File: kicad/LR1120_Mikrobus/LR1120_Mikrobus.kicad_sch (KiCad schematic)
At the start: 90 parts, among them Q1 NX2016SA-32M-EXS00A-CS06465, Q2 NT2016SA-32M-END4263A, Q3 NX3215SA, U1 LR1120, U2 SKY13588-460LF, U5 LIS2DE12, U7 M24128-BFMH6TG, U8 BGA524N6E6327XTSA1

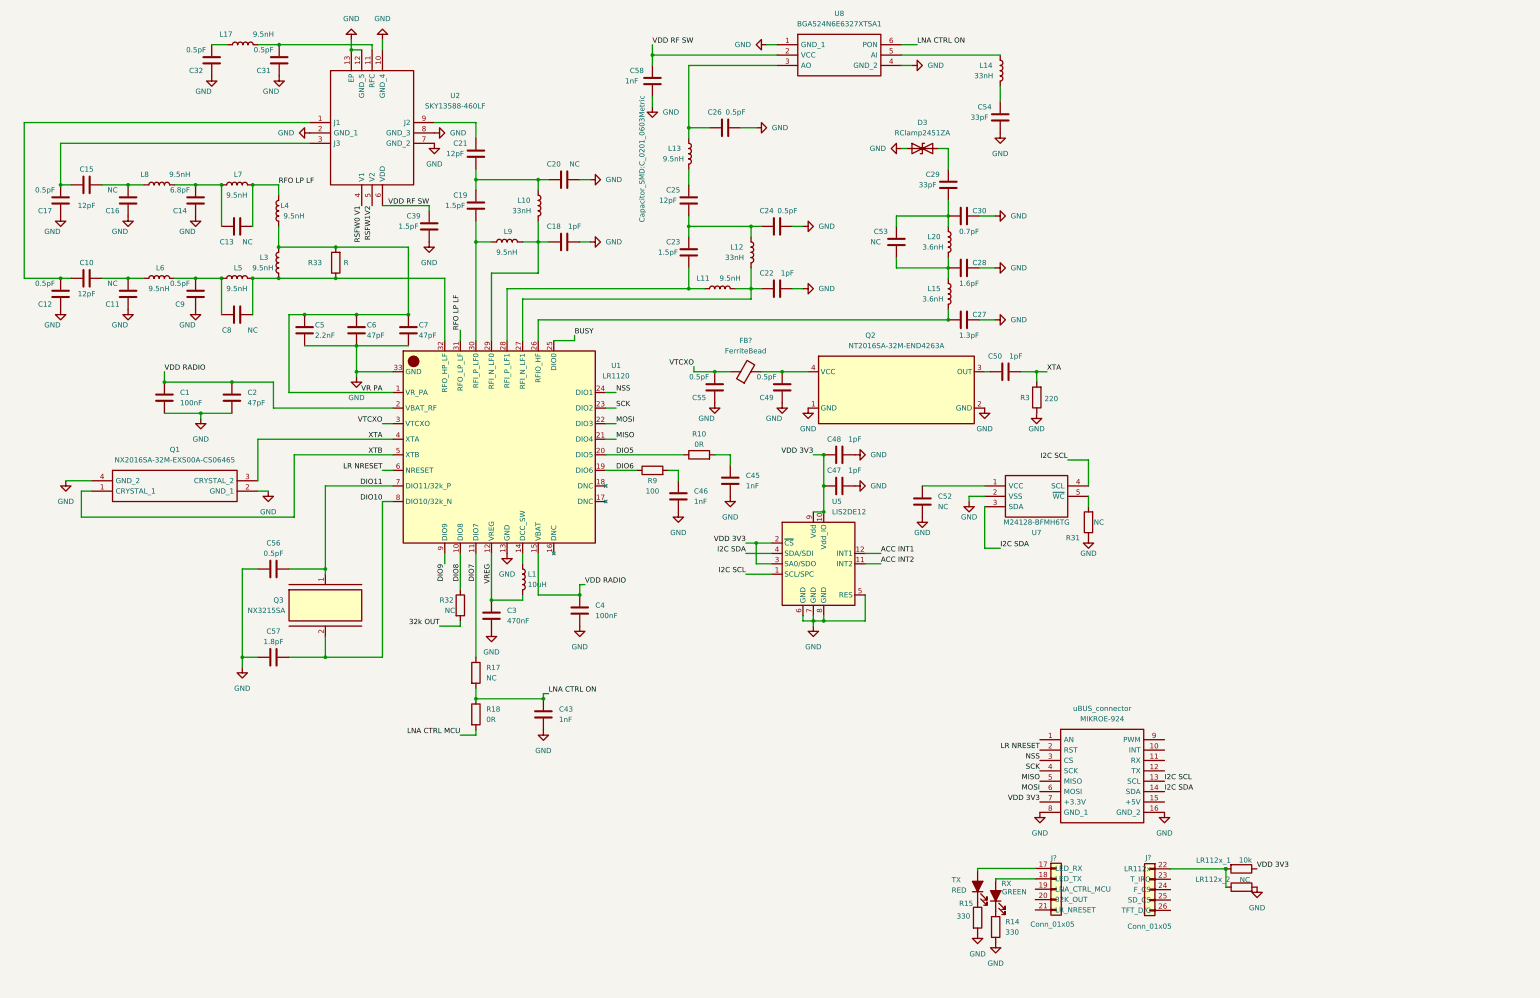
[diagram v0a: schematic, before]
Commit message: created board edges, added ant
Created board edges, placed antennas
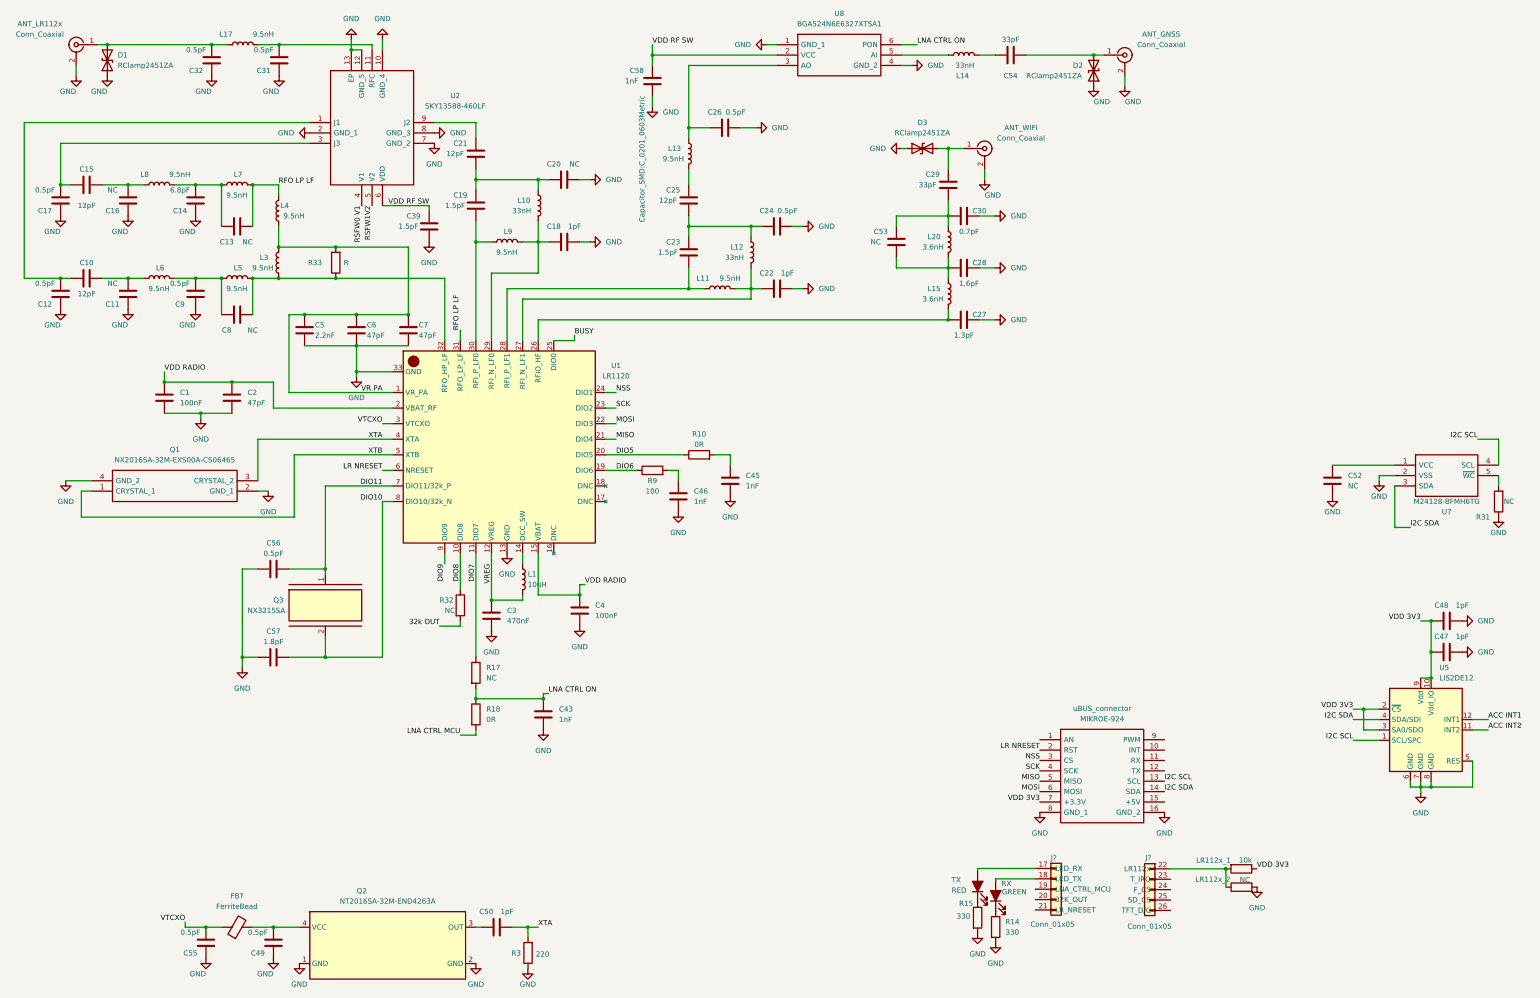
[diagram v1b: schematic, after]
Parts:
- added ANT_GNSS, ANT_LR112x, ANT_WIFI: Conn_Coaxial, Connector_Coaxial:U.FL_Hirose_U.FL-R-SMT-1_Vertical, symbol Connector:Conn_Coaxial
- added D1, D2: RClamp2451ZA, Diode_SMD:D_0201_0603Metric, symbol Device:D_TVS
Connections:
- net GND: now also ANT_GNSS.2 (Ext), ANT_LR112x.2 (Ext), ANT_WIFI.2 (Ext), D1.1 (A1), D2.1 (A1); no longer C54.1
- net at C32.1, L17.1: now also ANT_LR112x.1 (In), D1.2 (A2)
- net at C29.2, D3.2 (A2): now also ANT_WIFI.1 (In)
- new net: ANT_GNSS.1 (In), C54.1, D2.2 (A2)
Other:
- moved on the sheet: C47, C48, C49, C50, C52, C54, C55, FB?, L14, Q2, R3, R31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

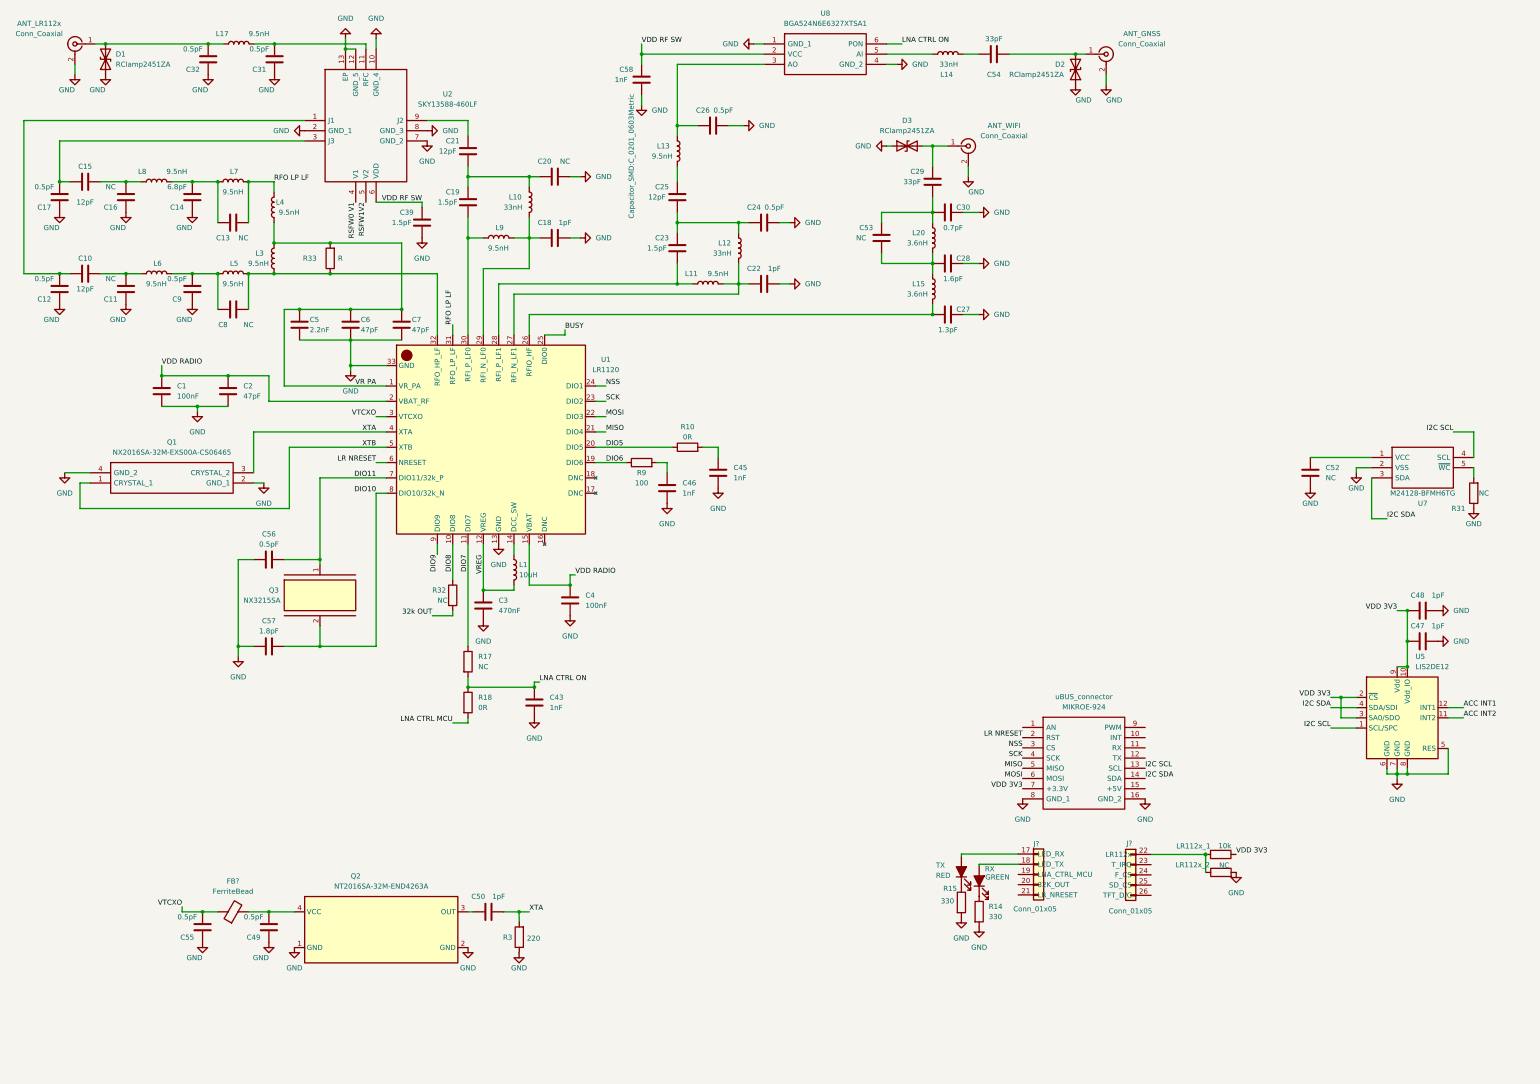
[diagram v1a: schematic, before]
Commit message: all components placed
all components have been placed. some footprints remain to be properly setup
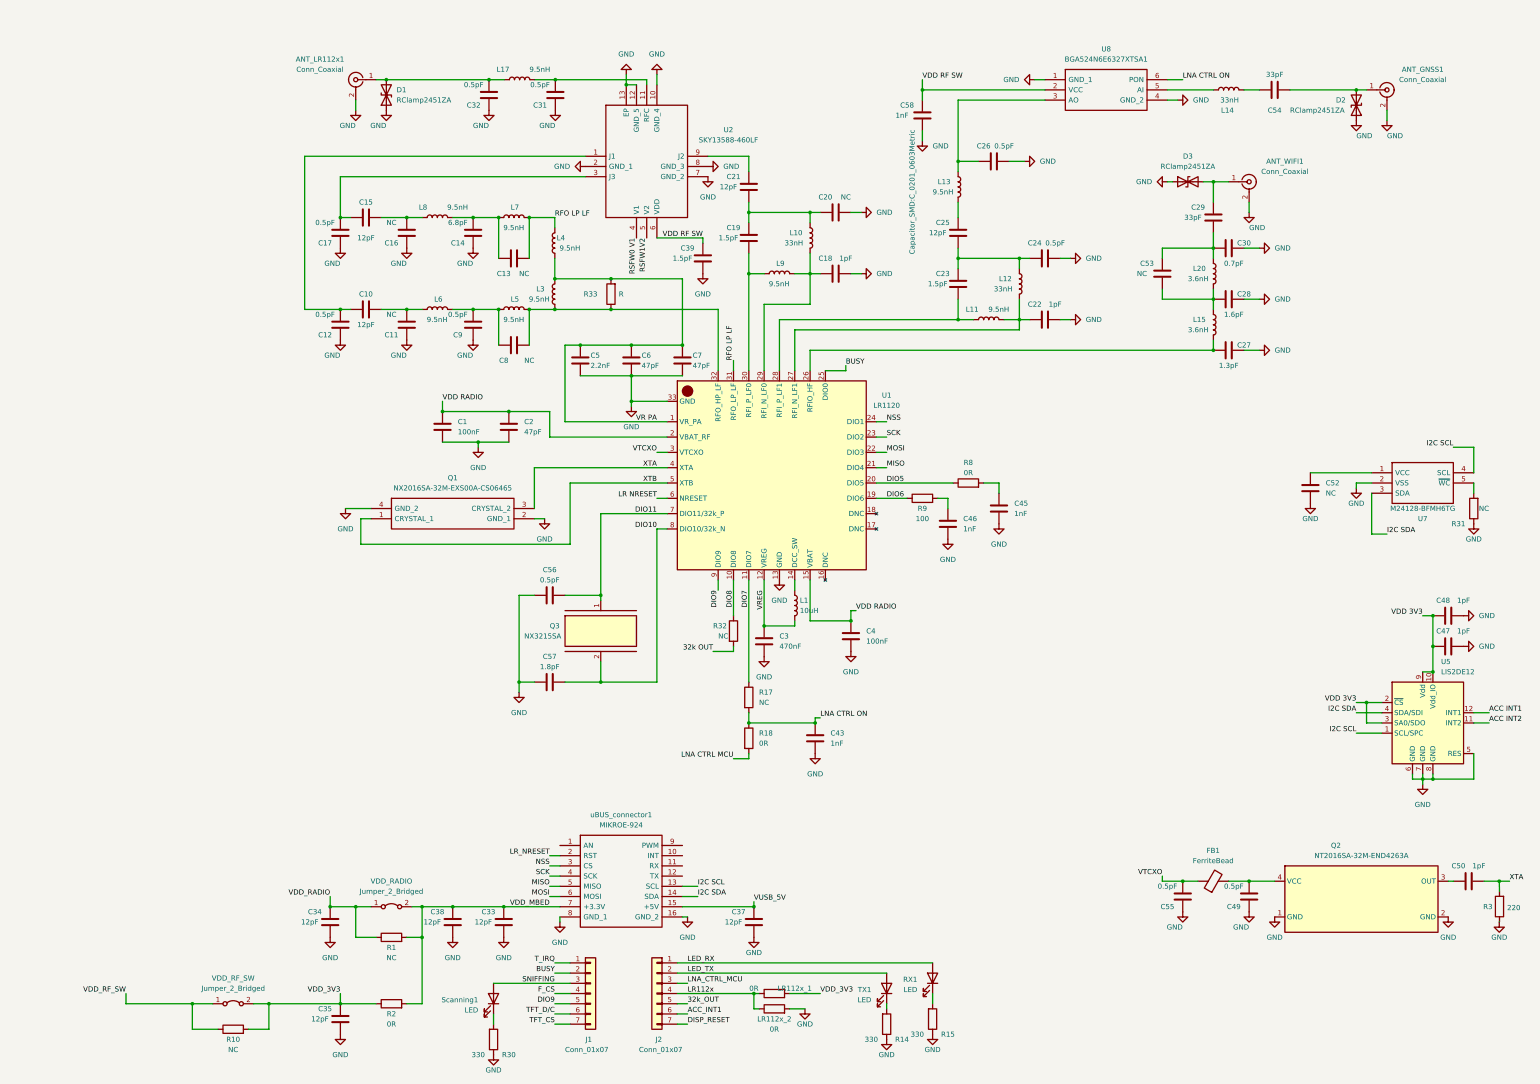
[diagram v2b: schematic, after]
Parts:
- removed J? (x2): Conn_01x05, symbol Connector_Generic:Conn_01x05
- removed RX: GREEN, symbol Device:LED_ALT
- removed TX: RED, symbol Device:LED_ALT
- added C33, C34, C35, C37, C38: 12pF, Capacitor_SMD:C_01005_0402Metric, symbol Device:C
- added J1, J2: Conn_01x07, symbol Connector_Generic:Conn_01x07
- added R1, R10: NC, Resistor_SMD:R_0201_0603Metric, symbol Device:R
- added R2: 0R, Resistor_SMD:R_0201_0603Metric, symbol Device:R
- added R30: 330, Resistor_SMD:R_0201_0603Metric, symbol Device:R
- added RX1, Scanning1, TX1: LED, symbol Device:LED
- added VDD_RADIO, VDD_RF_SW: Jumper_2_Bridged, symbol Jumper:Jumper_2_Bridged
- LR112x_1: value 10k -> 0R; footprint (none) -> Resistor_SMD:R_0603_1608Metric
- LR112x_2: value NC -> 0R; footprint (none) -> Resistor_SMD:R_0603_1608Metric
- R14, R15: footprint (none) -> Resistor_SMD:R_0201_0603Metric
- gave numbers to parts that had none: 1
- renumbered ANT_GNSS to ANT_GNSS1, ANT_LR112x to ANT_LR112x1, ANT_WIFI to ANT_WIFI1, R10 to R8, uBUS_connector to uBUS_connector1
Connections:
- net BUSY: now also J1.2 (Pin_2)
- net DIO9: now also J1.5 (Pin_5)
- net GND: now also R14.1, R15.1, C33.1, C34.1, C35.1, C37.1, C38.1, R30.1; no longer R14.2, R15.2
- net LR NRESET: no longer uBUS_connector1.2 (RST)
- net VDD 3V3: no longer LR112x_1.1, uBUS_connector1.7 (+3.3V)
- net VUSB_5V: now reaches uBUS_connector1.15 (+5V)
- net VUSB_5V: now also C37.2
- net LR112x: now reaches LR112x_2.1
- net LR112x: now also LR112x_1.1, J2.4 (Pin_4); no longer LR112x_1.2
- new net: R14.2, TX1.1 (K)
- new net: R30.2, Scanning1.1 (K)
- new net: R15.2, RX1.1 (K)
- new net 32k_OUT: J2.5 (Pin_5)
- new net ACC_INT1: J2.6 (Pin_6)
- new net DISP_RESET: J2.7 (Pin_7)
- new net F_CS: J1.4 (Pin_4)
- new net LED_RX: J2.1 (Pin_1), RX1.2 (A)
- new net LED_TX: J2.2 (Pin_2), TX1.2 (A)
- new net LNA_CTRL_MCU: J2.3 (Pin_3)
- new net LR_NRESET: uBUS_connector1.2 (RST)
- new net SNIFFING: J1.3 (Pin_3), Scanning1.2 (A)
- new net TFT_CS: J1.7 (Pin_7)
- new net TFT_D/C: J1.6 (Pin_6)
- new net T_IRQ: J1.1 (Pin_1)
- new net VDD_3V3: C35.2, LR112x_1.2, R10.2, R2.1, VDD_RF_SW.2 (B)
- new net VDD_MBED: C33.2, C38.2, R1.2, R2.2, VDD_RADIO.2 (B), uBUS_connector1.7 (+3.3V)
- new net VDD_RADIO: C34.2, R1.1, VDD_RADIO.1 (A)
- new net VDD_RF_SW: R10.1, VDD_RF_SW.1 (A)
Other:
- moved on the sheet: ANT_GNSS1, ANT_LR112x1, ANT_WIFI1, C1, C10, C11, C12, C13, C14, C15, C16, C17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

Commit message: all footprints assigned
All footprints were properly assingned according to the original BOM.
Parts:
- added R5, R6: NC, Resistor_SMD:R_0201_0603Metric, symbol Device:R
- C10, C11, C12, C13, C14, C15, C16, C17, C18, C19, C20, C21, C22, C23, C24, C25, C26, C27, C28, C29, C30, C31, C32, C34, C35, C37, C48, C8, C9: footprint Capacitor_SMD:C_01005_0402Metric -> Capacitor_SMD:C_0402_1005Metric
- C33, C39, C47, C49, C50, C53, C54, C55: footprint Capacitor_SMD:C_01005_0402Metric -> Capacitor_SMD:C_0201_0603Metric
- C38: footprint Capacitor_SMD:C_01005_0402Metric -> Capacitor_SMD:C_0603_1608Metric
- FB1: footprint (none) -> Inductor_SMD:L_0201_0603Metric
- J1, J2: footprint (none) -> Connector_PinHeader_2.54mm:PinHeader_1x07_P2.54mm_Vertical
- L10, L11, L12, L13, L15, L17, L20, L3, L4, L5, L6, L7, L8, L9: footprint Inductor_SMD:L_01005_0402Metric -> Inductor_SMD:L_0402_1005Metric
- L14: footprint Inductor_SMD:L_01005_0402Metric -> Inductor_SMD:L_0201_0603Metric
- LR112x_1, LR112x_2: footprint Resistor_SMD:R_0603_1608Metric -> Resistor_SMD:R_0402_1005Metric
- R1, R10, R2: footprint Resistor_SMD:R_0201_0603Metric -> Resistor_SMD:R_0603_1608Metric
- R33: footprint (none) -> Resistor_SMD:R_0201_0603Metric
- R8: footprint Resistor_SMD:R_0603_1608Metric -> Resistor_SMD:R_0201_0603Metric
- RX1, Scanning1, TX1: footprint (none) -> LED_SMD:LED_0402_1005Metric
- VDD_RADIO1: renamed from VDD_RADIO; footprint (none) -> Connector_PinHeader_2.54mm:PinHeader_1x02_P2.54mm_Vertical
- VDD_RF_SW1: renamed from VDD_RF_SW; footprint (none) -> Connector_PinHeader_2.54mm:PinHeader_1x02_P2.54mm_Vertical
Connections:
- net 32k OUT is gone; now on net 32k_OUT: R32.2
- net ACC INT1 is gone; now on net ACC_INT1: U5.12 (INT1)
- net LNA CTRL MCU is gone; now on net LNA_CTRL_MCU: R18.2
- net LR NRESET is gone; now on net LR_NRESET: U1.6 (NRESET)
- net VDD 3V3 is gone; now on net VDD_3V3: C47.2, C48.2, U5.10 (Vdd_IO), U5.2 (~{CS}), U5.3 (SA0/SDO), U5.9 (Vdd)
- net VDD RADIO is gone; now on net VDD_RADIO: C1.1, C2.1, C4.1, U1.15 (VBAT), U1.2 (VBAT_RF)
- net VDD RF SW is gone; now on net VDD_RF_SW: C39.2, C58.2, U2.6 (VDD), U8.2 (VCC)
- net VDD_3V3: now also R5.2, R6.2
- net ACC INT2 renamed ACC_INT2
- net I2C SCL renamed I2C_SCL
- net I2C_SCL: now also R5.1
- net I2C SDA renamed I2C_SDA
- net I2C_SDA: now also R6.1
- net LNA CTRL ON renamed LNA_CTRL_ON
- net RFO LP LF renamed RFO_LP_LF
- net RSFW0 V1 renamed RSFW0_V1
- net VR PA renamed VR_PA
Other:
- note added: "LR1120 Mikrobus"

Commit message: PCB:populated comp placed connectors
Populated the PCB with all the components. Placed and locked the connectors
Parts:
- added CON1: MIKROBUS_MODULE_CONN, MIKROBUS_MODULE_CONN, symbol mikroBUS:MIKROBUS_MODULE_CONN
- uBUS_connector1: footprint KiCad:MIKROE924 -> Mikrobus:MIKROBUS_MODULE_CONN
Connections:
- net GND: now also CON1.P8 (GND1), CON1.P9 (GND2); no longer uBUS_connector1.16 (GND_2), uBUS_connector1.8 (GND_1)
- net I2C_SCL: now also CON1.P12 (SCL); no longer uBUS_connector1.13 (SCL)
- net I2C_SDA: now also CON1.P11 (SDA); no longer uBUS_connector1.14 (SDA)
- net LR_NRESET: now also CON1.P2 (RST); no longer uBUS_connector1.2 (RST)
- net MISO: now also CON1.P5 (MISO); no longer uBUS_connector1.5 (MISO)
- net MOSI: now also CON1.P6 (MOSI); no longer uBUS_connector1.6 (MOSI)
- net NSS: now also CON1.P3 (CS); no longer uBUS_connector1.3 (CS)
- net SCK: now also CON1.P4 (SCK); no longer uBUS_connector1.4 (SCK)
- net VDD_MBED: now also CON1.P7 (3V3); no longer uBUS_connector1.7 (+3.3V)
- net VUSB_5V: now also CON1.P10 (5V); no longer uBUS_connector1.15 (+5V)
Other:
- moved on the sheet: C33, C34, C35, C37, C38, J1, J2, LR112x_1, LR112x_2, R1, R10, R14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
